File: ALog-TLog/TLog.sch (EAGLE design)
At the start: 98 parts, among them IC1 ATMEGA644M, J6 5.5x2.1mm Barrel, Q1 MOSFET-NCH-BSS138, Q5 MOSFET_PCH-IRLML2244, Q6 MOSFET_PCH-IRLML2244, Q7 MOSFET_PCH-IRLML2244, Q8 MOSFET-NCH-BSS138, Q9 MOSFET-NCH-BSS138, U2 FT231X-Q, U3 915MHz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

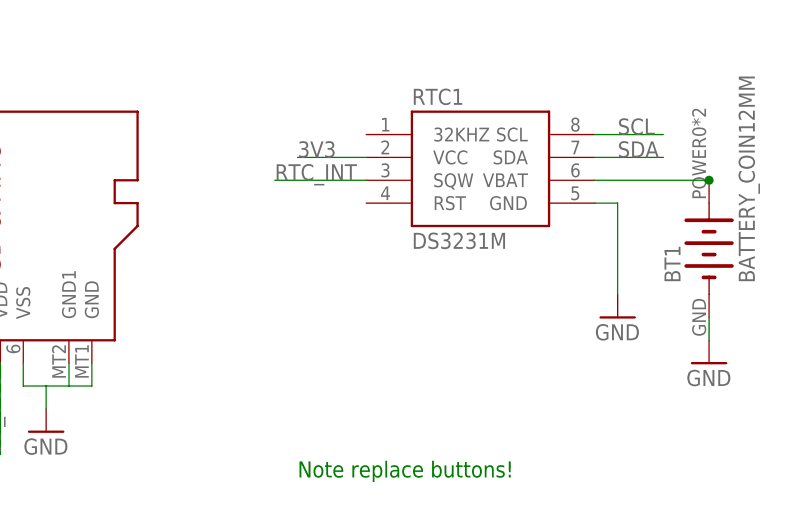
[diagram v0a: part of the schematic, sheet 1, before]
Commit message: Changed part number for ATMEGA644P
Fixed the part and digikey numbers, was ATMEGA644A, now ATMEGA644PA
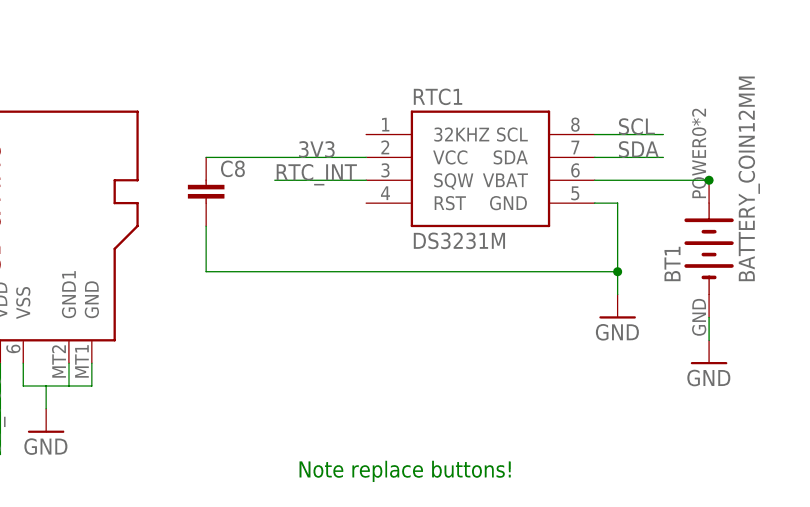
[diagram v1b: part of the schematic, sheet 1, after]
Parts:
- added C8: (no value), bschulz:C-EUC0603
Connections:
- net 3V3: now also C8.1
- net GND: now also C8.2
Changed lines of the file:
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@@
 <?xml version="1.0" encoding="utf-8"?>
 <!DOCTYPE eagle SYSTEM "eagle.dtd">
-<eagle version="8.3.0">
+<eagle version="8.3.2">
 <drawing>
 <settings>
@@
 <part name="GND7" library="SparkFun-PowerSymbols" library_urn="urn:adsk.eagle:library:530" deviceset="GND" device=""/>
 <part name="C7" library="bschulz" deviceset="C-EU" device="C0805" technology="10UF" value="10uF"/>
+<part name="C8" library="bschulz" deviceset="C-EU" device="C0603"/>
 </parts>
 <sheets>
@@
 </instance>
 <instance part="C6" gate="G$1" x="30.48" y="132.08" rot="R90"/>
+<instance part="C8" gate="G$1" x="73.66" y="205.74"/>
 </instances>
 <busses>
@@
 <segment>
 <pinref part="RTC1" gate="G$1" pin="VCC"/>
-<wire x1="91.44" y1="208.28" x2="83.82" y2="208.28" width="0.1524" layer="91"/>
 <label x="83.82" y="208.28" size="1.778" layer="95"/>
+<pinref part="C8" gate="G$1" pin="1"/>
+<wire x1="73.66" y1="208.28" x2="91.44" y2="208.28" width="0.1524" layer="91"/>
 </segment>
 <segment>
@@
 <pinref part="GND25" gate="1" pin="GND"/>
 <wire x1="116.84" y1="203.2" x2="119.38" y2="203.2" width="0.1524" layer="91"/>
-<wire x1="119.38" y1="203.2" x2="119.38" y2="193.04" width="0.1524" layer="91"/>
-</segment>
-<segment>
+<wire x1="119.38" y1="203.2" x2="119.38" y2="195.58" width="0.1524" layer="91"/>
+<pinref part="C8" gate="G$1" pin="2"/>
+<wire x1="119.38" y1="195.58" x2="119.38" y2="193.04" width="0.1524" layer="91"/>
+<wire x1="73.66" y1="200.66" x2="73.66" y2="195.58" width="0.1524" layer="91"/>
+<wire x1="73.66" y1="195.58" x2="119.38" y2="195.58" width="0.1524" layer="91"/>
+<junction x="119.38" y="195.58"/>
+</segment>
+<segment>

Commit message: add gerber files and make some BOM improvements
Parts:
- C18: value .1uF -> 0.1uF
- C25, C5: device rcl:C-EUC0603 -> bschulz:C-EU12PFC0603
- J9: MF On Shore Technology -> On Shore Technology
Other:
- moved on the sheet: J10, J8, J9

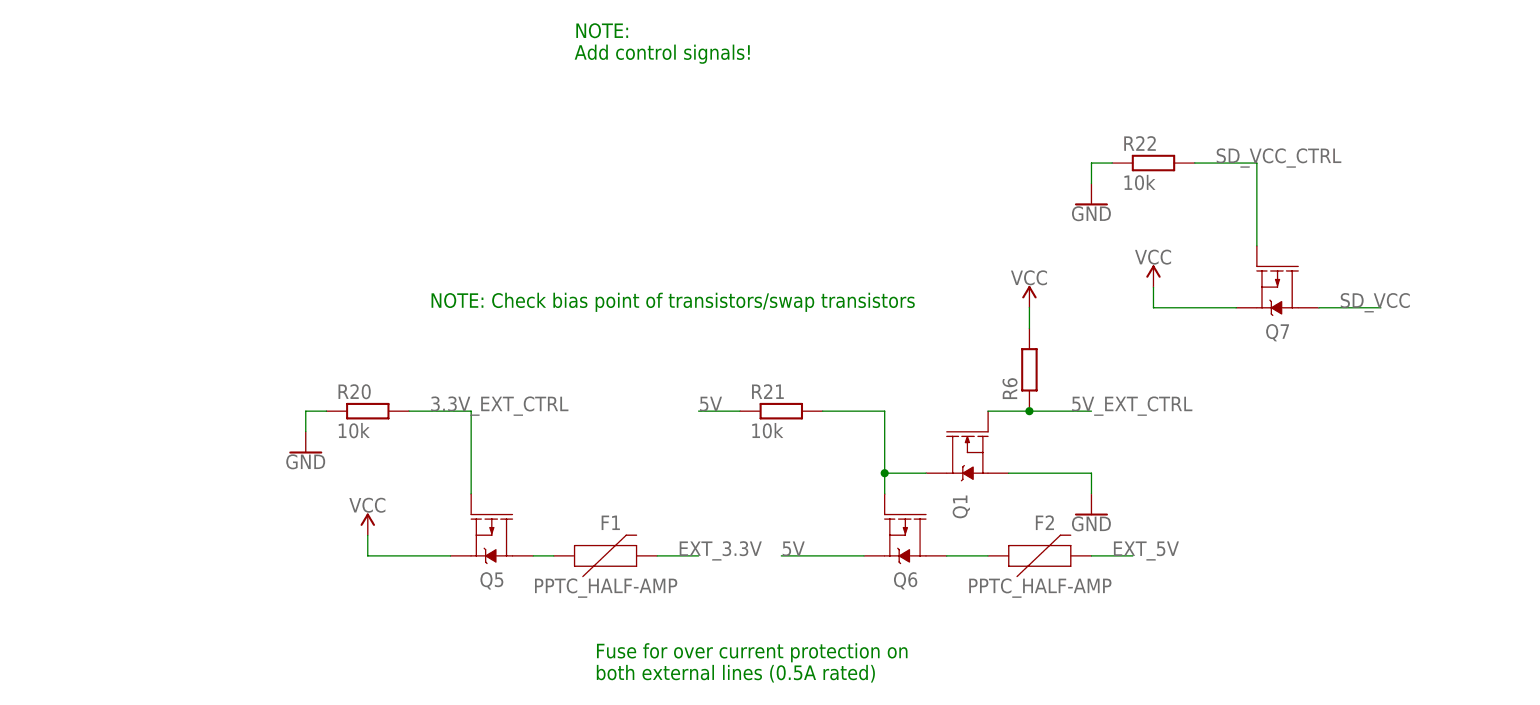
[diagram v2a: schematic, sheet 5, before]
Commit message: Added Gate Drivers, Fixed Basic Issues
Added gate drievrs to all MOSFETs, also broke out battery voltage to screw terminals, and increased size of push button pads to improve reflow
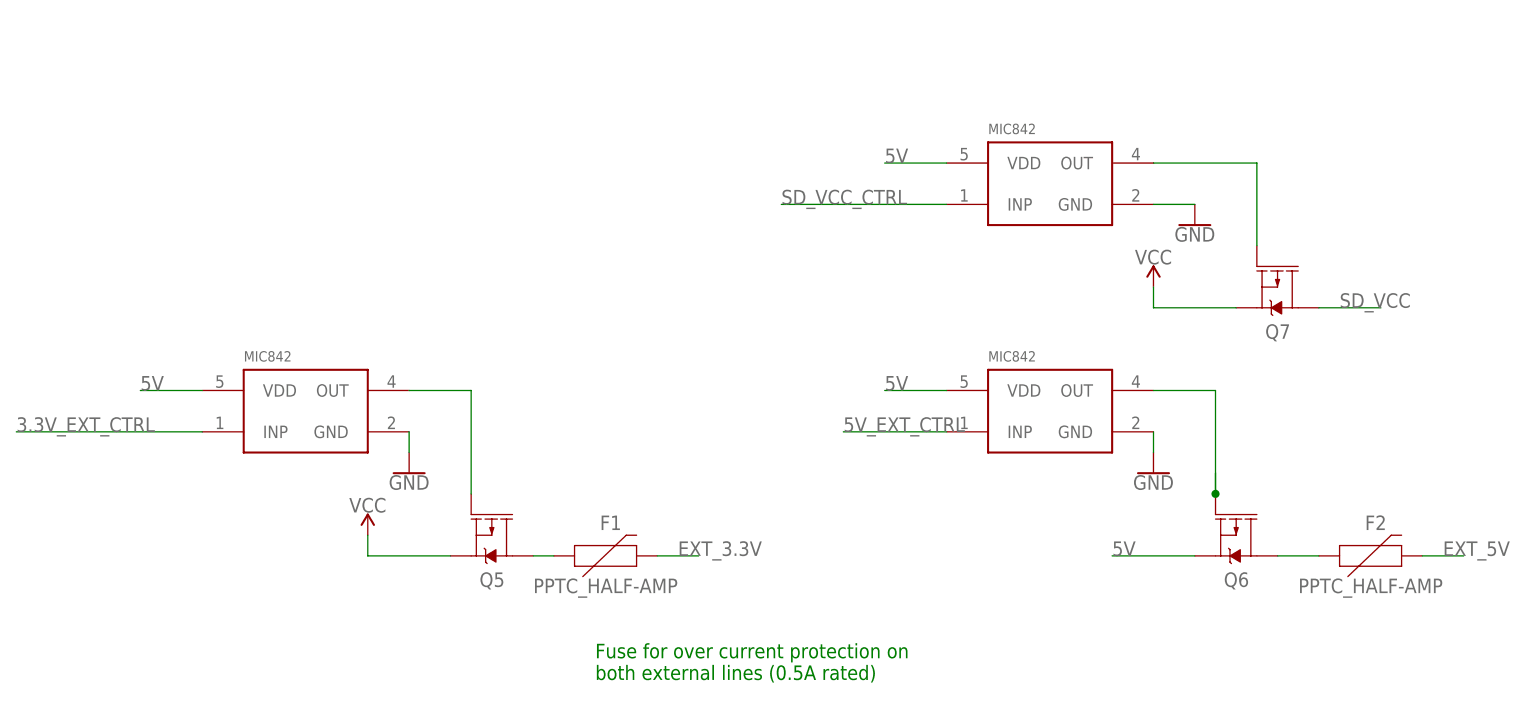
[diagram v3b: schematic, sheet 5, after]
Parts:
- removed Q1: MOSFET-NCH-BSS138, bschulz:MOSFET-NCH-BSS138
- removed R20, R21, R22: 10k, bschulz:R-EU_10KR0603
- removed R6: (no value), bschulz:R-EU_10KR0603
- added U$17, U$18, U$19: MIC842, bschulz:MIC842
- U$5, U$9: value SWITCHC&K_400GF -> BUTTON4.2X3.2; device bschulz:SWITCHC&K_400GF -> bschulz:BUTTON4.2X3.2
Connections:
- new net N$1: Q5.G, U$18.OUT
- new net N$3: Q7.G, U$19.OUT
- net 3.3V_EXT_CTRL: now also U$18.INP; no longer Q5.G, R20.2
- net 3V3: no longer R6.2
- net 5V: now also U$17.VDD, U$18.VDD, U$19.VDD; no longer R21.1
- net 5V_EXT_CTRL: now also U$17.INP; no longer Q1.G, R6.1
- net BATT: now also J10.8
- net EXT_3.3V: no longer J10.8
- net GND: now also U$17.GND, U$18.GND, U$19.GND; no longer Q1.S, R20.1, R22.1
- net N$30: now also U$17.OUT; no longer Q1.D, R21.2
- net SD_VCC_CTRL: now also U$19.INP; no longer Q7.G, R22.2
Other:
- note removed: "NOTE: Add control signals!"
- note removed: "NOTE: Check bias point of transistors/swap transistors"
- moved on the sheet: F2, Q6
